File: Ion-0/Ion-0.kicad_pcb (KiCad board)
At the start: 4 copper layers, 54.6 x 86.4 mm, 96 parts, among them J1 Beaglebone-green-P9, J11 Conn_Prob_1, J12 Conn_Prob_2, J2 Beaglebone-green-P8, J3 Conn_02x06_Odd_Even, J4 Conn_02x06_Odd_Even, J5 Conn_02x06_Odd_Even, J6 Coaxial_Small, J8 Conn_Heater, J9 Conn_prob_3, Q1 IRLML6244, Q2 IRLML6244, U1 HDC2080, U2 MS5607-02BA, U3 BNO085, U4 TCA9617ADGKR, U6 MAX-M10M-00B, U7 TPS3850H50DRCR, U8 SN65HVD230, Y2 9HT10-32.768KBZF-T

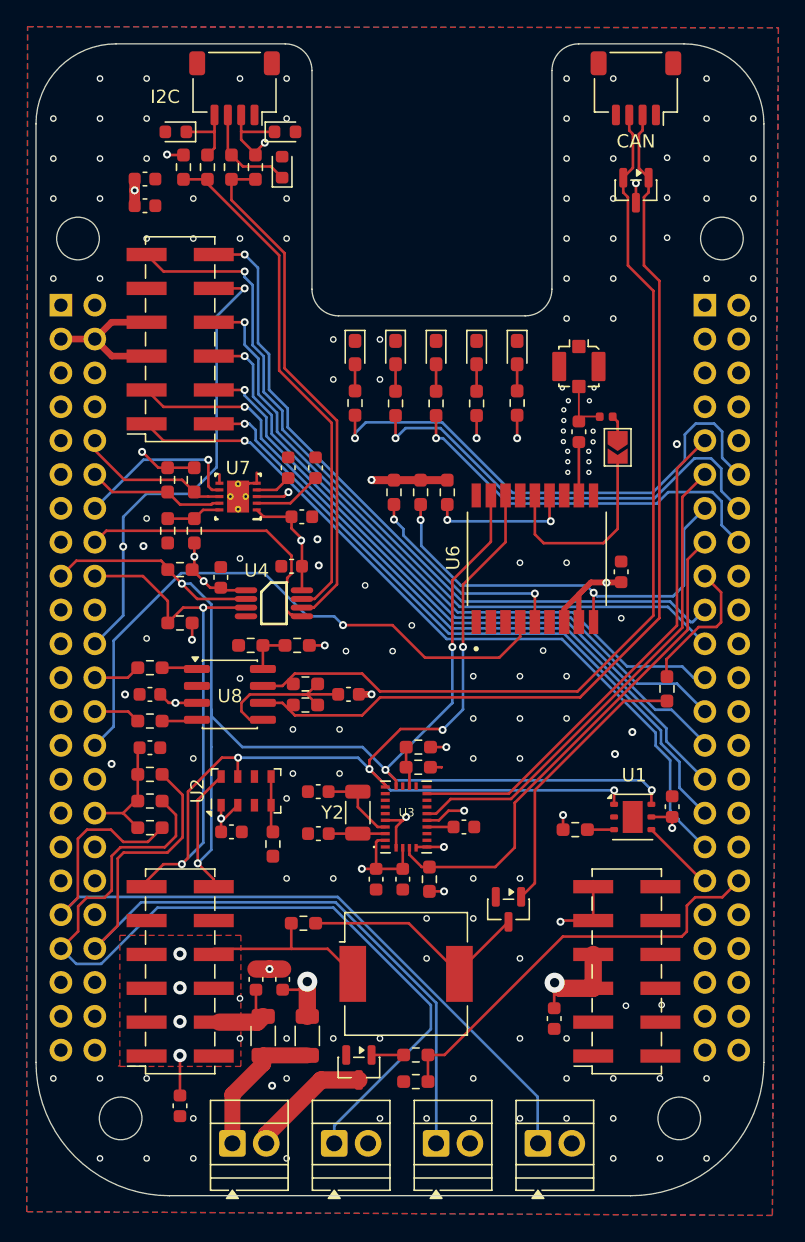
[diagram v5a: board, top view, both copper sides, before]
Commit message: version 0.8 - stepper driver included and better detailled schematic
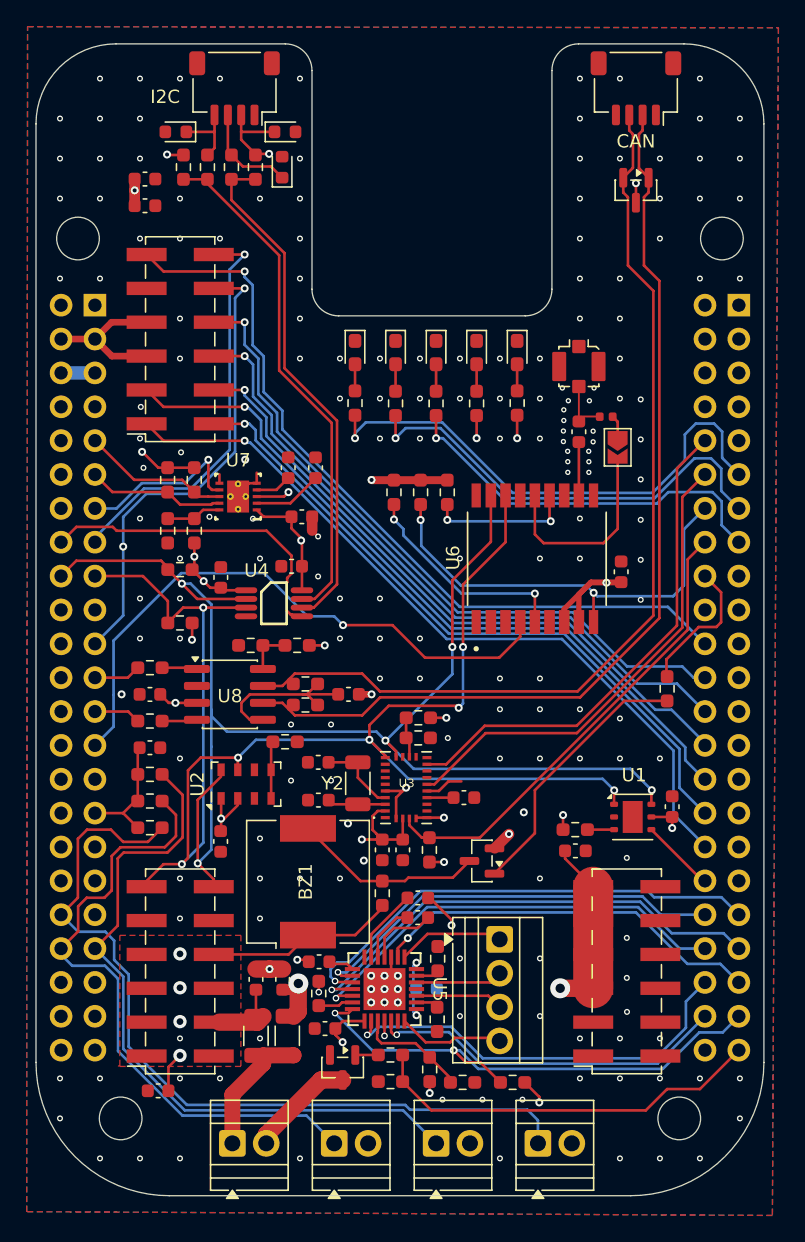
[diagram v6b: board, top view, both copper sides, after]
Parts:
- added C25: 100nF, Capacitor_SMD:C_0603_1608Metric, F.Cu at (149.8, 122.9)
- added C26: 100nF, Capacitor_SMD:C_0603_1608Metric, F.Cu at (149.8, 121.5)
- added C27: 0.22uF, Capacitor_SMD:C_0603_1608Metric, F.Cu at (142.9, 131.3)
- added C28: 0.22uF, Capacitor_SMD:C_0603_1608Metric, F.Cu at (142.4, 126.2)
- added C29: 100uF, Capacitor_SMD:C_0603_1608Metric, B.Cu at (150.5, 128.3)
- added J15: Conn_01x04, TerminalBlock:TerminalBlock_Xinya_XY308-2.54-4P_1x04_P2.54mm_Horizontal, F.Cu at (156.0, 124.6)
- added R19: 5K, Resistor_SMD:R_0603_1608Metric_Pad0.98x0.95mm_HandSolder, F.Cu at (156.9, 135.3)
- added R20: 20K, Resistor_SMD:R_0603_1608Metric_Pad0.98x0.95mm_HandSolder, F.Cu at (142.4, 128.6)
- added R43: 0.05, Resistor_SMD:R_0603_1608Metric_Pad0.98x0.95mm_HandSolder, F.Cu at (151.3, 126.0)
- added R44: 0.05, Resistor_SMD:R_0603_1608Metric_Pad0.98x0.95mm_HandSolder, F.Cu at (151.3, 130.6)
- added R45: 330, Resistor_SMD:R_0603_1608Metric_Pad0.98x0.95mm_HandSolder, F.Cu at (147.2, 121.1)
- added R46: 330, Resistor_SMD:R_0603_1608Metric_Pad0.98x0.95mm_HandSolder, F.Cu at (168.5, 105.8)
- added U5: A4988SETTR-T, 1_Ion:QFN-28_ALM, F.Cu at (147.3, 128.3)
- BZ1: value buzzer -> Buzzer
- R21: value 330 -> 33K
- R22: value 330 -> 10K
- moved R22 33.3 mm to (153.2, 135.3), turned to 0 degrees
- moved R21 14.5 mm to (150.7, 134.3), turned to 90 degrees
- moved C14 12.7 mm to (161.7, 117.9), turned to 0 degrees
- moved BZ1 10.1 mm to (141.6, 120.2), turned to 90 degrees
- moved R42 7.72 mm to (139.9, 109.8), turned to 0 degrees
- moved G*** 5.64 mm to (148.5, 99.4)
- moved Q1 4.14 mm to (154.7, 118.7), turned to 180 degrees
- moved C2 2.52 mm to (142.4, 114.1)
- moved C4 2.25 mm to (147.2, 117.9)
- moved C5 2.20 mm to (148.7, 117.9)
- moved C6 2.20 mm to (153.3, 113.9)
- moved R10 2.20 mm to (149.9, 109.5)
- moved R8 2.20 mm to (150.7, 117.9)
- moved R9 2.20 mm to (149.9, 108.0)
- moved U3 2.20 mm to (149.0, 113.2)
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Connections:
- net /GPIO_51 renamed /I2C1B-EN
- C23 pad 1: +1V8 -> GND
- C23 pad 2: GND -> +1V8
- J1 pad 10: /~{SYS_RST} -> unconnected-(J1-Pin_10-Pad10)
- J1 pad 11: unconnected-(J1-Pin_11-Pad11) -> /~{WD-RST}
- J1 pad 12: /GPIO_60 -> unconnected-(J1-Pin_12-Pad12)
- J1 pad 13: unconnected-(J1-Pin_13-Pad13) -> /WD-INT
- J1 pad 14: /GPIO_50 -> unconnected-(J1-Pin_14-Pad14)
- J1 pad 15: unconnected-(J1-Pin_15-Pad15) -> /LED_PWM_2
- J1 pad 17: /I2C1_SCL -> /I2C1_SDA
- J1 pad 18: /I2C1_SDA -> /I2C1_SCL
- J1 pad 21: unconnected-(J1-Pin_21-Pad21) -> /LED_PWM_1
- J1 pad 22: /LED_PWM_1 -> unconnected-(J1-Pin_22-Pad22)
- J1 pad 23: unconnected-(J1-Pin_23-Pad23) -> /CAN_TXD
- J1 pad 24: /CAN_TXD -> unconnected-(J1-Pin_24-Pad24)
- J1 pad 25: unconnected-(J1-Pin_25-Pad25) -> /CAN_RXD
- J1 pad 26: /CAN_RXD -> unconnected-(J1-Pin_26-Pad26)
- J1 pad 27: unconnected-(J1-Pin_27-Pad27) -> /GPS-PPS
- J1 pad 28: /ECAPPWM2 -> unconnected-(J1-Pin_28-Pad28)
- J1 pad 31: unconnected-(J1-Pin_31-Pad31) -> +1V8
- J1 pad 32: +1V8 -> unconnected-(J1-Pin_32-Pad32)
- J1 pad 33: unconnected-(J1-Pin_33-Pad33) -> GND
- J1 pad 34: GND -> unconnected-(J1-Pin_34-Pad34)
- J1 pad 37: /AIN2 -> unconnected-(J1-Pin_37-Pad37)
- J1 pad 38: unconnected-(J1-Pin_38-Pad38) -> /AIN2
- J1 pad 39: /AIN0 -> /AIN1
- J1 pad 40: /AIN1 -> /AIN0
- J1 pad 9: unconnected-(J1-Pin_9-Pad9) -> /~{SYS_RST}
- J2 pad 10: unconnected-(J2-Pin_10-Pad10) -> /~{BNO-INT}
- J2 pad 11: /GPIO_32 -> /IND-2
- J2 pad 12: /GPIO_76 -> /~{BNO-RST}
- J2 pad 13: /GPIO_69 -> /IND-1
- J2 pad 14: /GPIO_74 -> /~{GPS-RST}
- J2 pad 15: /GPIO_62 -> /STATE-LED
- J2 pad 16: /GPIO_72 -> /~{BNO-BOOT}
- J2 pad 17: /GPIO_86 -> unconnected-(J2-Pin_17-Pad17)
- J2 pad 18: unconnected-(J2-Pin_18-Pad18) -> /Buzzer
- J2 pad 19: /LED_PWM_2 -> unconnected-(J2-Pin_19-Pad19)
- J2 pad 21: /IND_3 -> unconnected-(J2-Pin_21-Pad21)
- J2 pad 22: unconnected-(J2-Pin_22-Pad22) -> /IND_3
- J2 pad 23: /MOTOR_2_A -> unconnected-(J2-Pin_23-Pad23)
- J2 pad 24: unconnected-(J2-Pin_24-Pad24) -> /MOTOR_2_A
- J2 pad 25: /MOTOR_2_B -> unconnected-(J2-Pin_25-Pad25)
- J2 pad 26: unconnected-(J2-Pin_26-Pad26) -> /MOTOR_2_B
- J2 pad 27: /MOTOR_1_A -> unconnected-(J2-Pin_27-Pad27)
- J2 pad 28: unconnected-(J2-Pin_28-Pad28) -> /MOTOR_1_A
- J2 pad 29: /SERVO_1 -> unconnected-(J2-Pin_29-Pad29)
- J2 pad 30: unconnected-(J2-Pin_30-Pad30) -> /SERVO_1
- J2 pad 31: /MOTOR_1_B -> unconnected-(J2-Pin_31-Pad31)
- J2 pad 32: unconnected-(J2-Pin_32-Pad32) -> /MOTOR_1_B
- J2 pad 33: /SERVO_2 -> unconnected-(J2-Pin_33-Pad33)
- J2 pad 34: unconnected-(J2-Pin_34-Pad34) -> /SERVO_2
- J2 pad 35: /GPIO_8 -> unconnected-(J2-Pin_35-Pad35)
- J2 pad 36: /EHRPWM1B -> /Humidity-INT
- J2 pad 37: unconnected-(J2-Pin_37-Pad37) -> /STP-MS2
- J2 pad 38: unconnected-(J2-Pin_38-Pad38) -> /STP-MS1
- J2 pad 39: unconnected-(J2-Pin_39-Pad39) -> /STP-MS3
- J2 pad 40: unconnected-(J2-Pin_40-Pad40) -> /~{STP-RST}
- J2 pad 41: unconnected-(J2-Pin_41-Pad41) -> /~{STP-EN}
- J2 pad 42: unconnected-(J2-Pin_42-Pad42) -> /STP-STEP
- J2 pad 43: unconnected-(J2-Pin_43-Pad43) -> /~{STP-SLP}
- J2 pad 44: unconnected-(J2-Pin_44-Pad44) -> /STP-DIR
- J2 pad 45: unconnected-(J2-Pin_45-Pad45) -> /PWM-Heaters
- J2 pad 9: /GPIO_36 -> unconnected-(J2-Pin_9-Pad9)
- R11 pad 1: /EHRPWM1B -> /PWM-Heaters
- R14 pad 2: /GPIO_60 -> /~{WD-RST}
- R17 pad 2: /GPIO_69 -> /~{GPS-RST}
- R21 pad 1: +5V -> +3V3
- R21 pad 2: Net-(BZ1--) -> Net-(U5-REF)
- R22 pad 1: /GPIO_86 -> Net-(U5-REF)
- R22 pad 2: Net-(Q1-G) -> GND
- R29 pad 1: /EHRPWM1B -> /PWM-Heaters
- R32 pad 1: /GPIO_72 -> /STATE-LED
- R33 pad 1: /GPIO_74 -> /IND-1
- R34 pad 1: /GPIO_76 -> /IND-2
- R8 pad 2: /GPIO_62 -> /~{BNO-BOOT}
- U1 pad 4: /GPIO_8 -> /Humidity-INT
- U3 pad 11: /GPIO_32 -> /~{BNO-RST}
- U3 pad 14: /GPIO_36 -> /~{BNO-INT}
- U3 pad 4: /GPIO_62 -> /~{BNO-BOOT}
- U6 pad 4: /ECAPPWM2 -> /GPS-PPS
- U6 pad 9: /GPIO_69 -> /~{GPS-RST}
- U7 pad 7: /GPIO_50 -> /WD-INT
- U7 pad 9: /GPIO_60 -> /~{WD-RST}
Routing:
- net /GPS-PPS: track 0.00 -> 45.4 mm, vias 0 -> 1
- net /ECAPPWM2: track 45.4 -> 0.00 mm, vias 1 -> 0
- net /~{STP-SLP}: track 0.00 -> 39.6 mm, vias 0 -> 2
- net /IND-2: track 0.00 -> 39.4 mm, vias 0 -> 1
- net /GPIO_76: track 39.4 -> 0.00 mm, vias 1 -> 0
- net /GPIO_36: track 38.7 -> 0.00 mm
- net /GPIO_62: track 38.2 -> 0.00 mm
- net /~{BNO-INT}: track 0.00 -> 37.8 mm
- net /GPIO_32: track 37.3 -> 0.00 mm
- net /STP-MS3: track 0.00 -> 37.1 mm, vias 0 -> 1
- net /~{BNO-RST}: track 0.00 -> 36.3 mm
- net /STP-MS2: track 0.00 -> 36.2 mm, vias 0 -> 1
- net /~{BNO-BOOT}: track 0.00 -> 35.3 mm
- net /IND-1: track 0.00 -> 33.7 mm, vias 0 -> 1
- net /GPIO_74: track 33.7 -> 0.00 mm, vias 1 -> 0
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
